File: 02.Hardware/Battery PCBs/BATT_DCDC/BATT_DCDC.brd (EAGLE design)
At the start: 30.4 x 23.5 mm, 66 parts, among them K3 FLEX8, Q1 NVTFS9D6P04M8LTAG, Q2 2N7002PW, Q5 2N7002PW, U1 MCP6071T-E/OT, U3 TPS55330RTET, U7 TPIC2810D

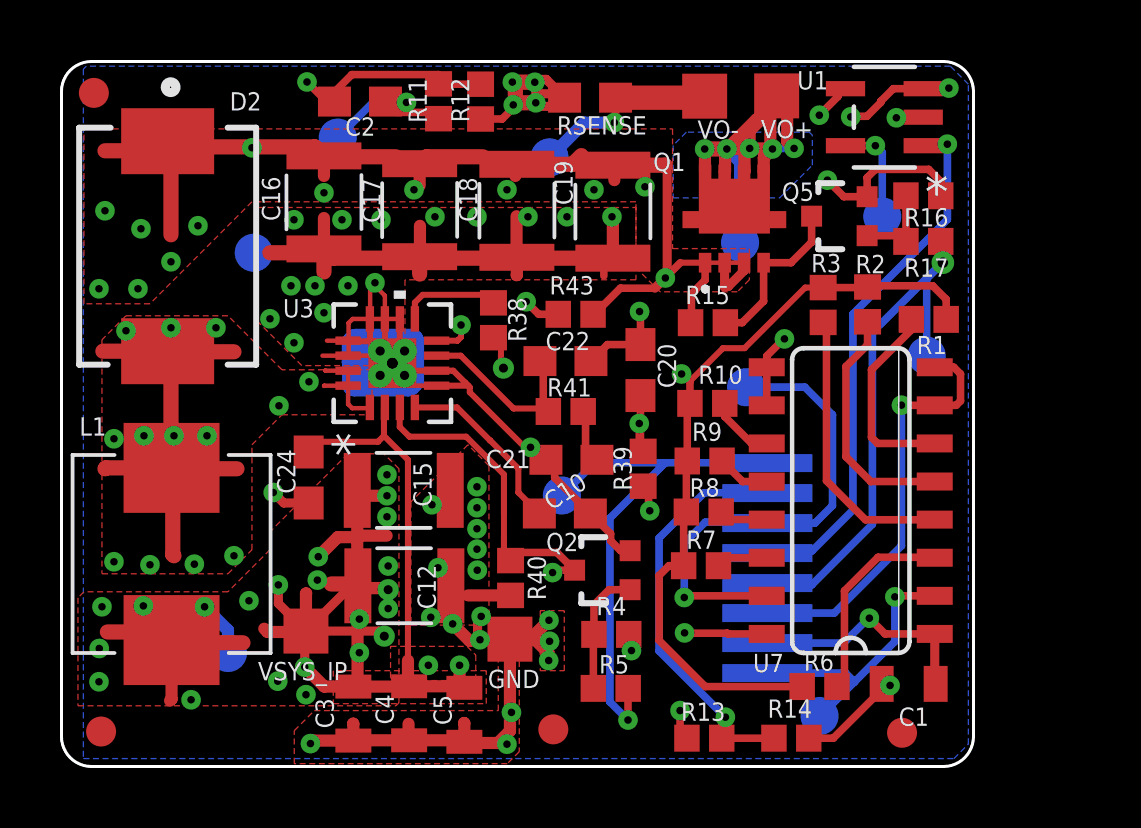
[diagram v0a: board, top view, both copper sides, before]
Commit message: Cambios revisados con David
Revision de los pcbs de la bateria.

En el DCDC se añade un diode Clamp (bat54s) en la medicion de la tension de salida.
Actualizacion de la BOM a v8.
Documentos de Cambios de versiones
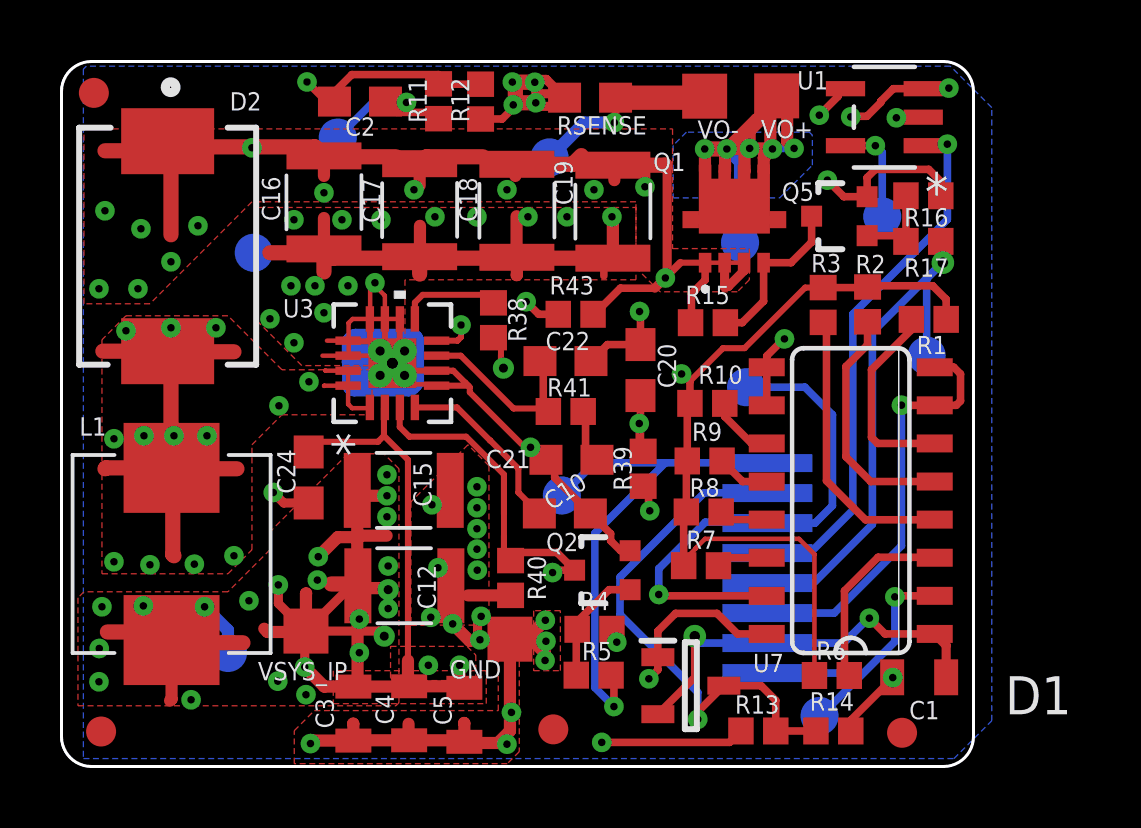
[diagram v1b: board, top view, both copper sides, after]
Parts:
- added D1: BAT54S, BAT54S:SOT95P240X110-3N
- R11: value 15k -> 5k1
- R12: value 1k -> 8k2
- RSENSE: value 10mR -> 100mR
- moved R13 1.82 mm to (44.8, 4.39)
- moved R14 1.42 mm to (47.3, 4.39)
- moved R5 0.72 mm to (39.3, 6.25)
- moved R4 0.59 mm to (39.3, 7.78)
- moved R6 0.55 mm to (47.2, 6.24)
- moved C1 0.41 mm to (50.1, 6.18)
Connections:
- net GND: now also D1.1
- net VCC: now also D1.2
- net VOUTSENSE: now also D1.3
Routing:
- net VOUT+: track 47.2 -> 55.9 mm
- net VCC: track 27.2 -> 32.7 mm, vias 2 -> 3
- net VOUTSENSE: track 13.6 -> 17.7 mm
- net GND: track 138.7 -> 140.5 mm
- net SCL: track 16.4 -> 17.5 mm

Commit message: Review final antes de produccion
-cambian valores de c10, r13, r15
-se añaden notas
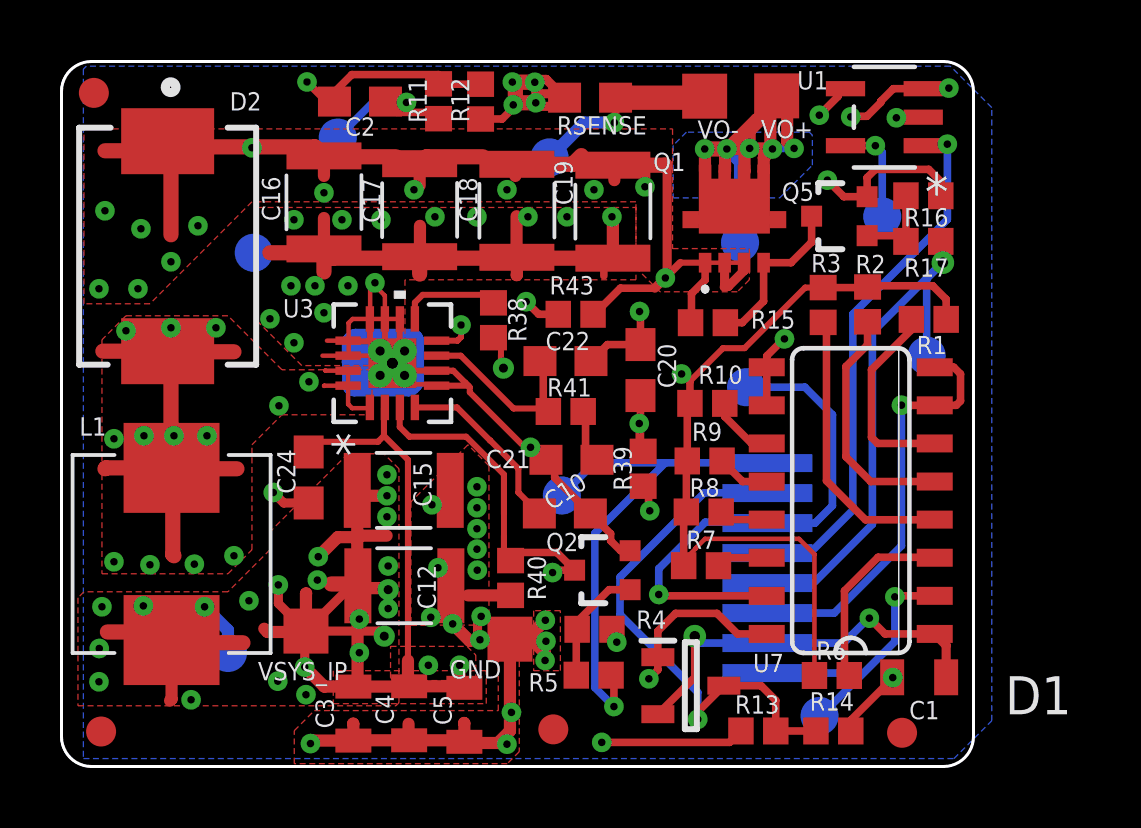
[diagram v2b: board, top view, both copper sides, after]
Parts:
- C20: value 47nF -> N.A.
- R13: value 150k -> 169k
- R15: value 470k -> 120k
- R40: value 78.7k -> N.A.
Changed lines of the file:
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@@
 <drawing>
 <settings>
-<setting alwaysvectorfont="no"/>
+<setting alwaysvectorfont="yes"/>
 <setting keepoldvectorfont="yes"/>
 <setting verticaltext="up"/>
@@
 <grid distance="0.01" unitdist="mm" unit="mm" style="lines" multiple="1" display="yes" altdistance="0.1" altunitdist="mm" altunit="mm"/>
 <layers>
-<layer number="1" name="Top" color="4" fill="1" visible="no" active="yes"/>
-<layer number="2" name="Route2" color="1" fill="3" visible="yes" active="yes"/>
+<layer number="1" name="Top" color="4" fill="1" visible="yes" active="yes"/>
+<layer number="2" name="Route2" color="1" fill="3" visible="no" active="yes"/>
 <layer number="3" name="Route3" color="4" fill="3" visible="no" active="no"/>
 <layer number="4" name="Route4" color="1" fill="4" visible="no" active="no"/>
@@
 <layer number="13" name="Route13" color="4" fill="5" visible="no" active="no"/>
 <layer number="14" name="Route14" color="1" fill="6" visible="no" active="no"/>
-<layer number="15" name="Route15" color="4" fill="6" visible="yes" active="yes"/>
+<layer number="15" name="Route15" color="4" fill="6" visible="no" active="yes"/>
 <layer number="16" name="Bottom" color="1" fill="1" visible="no" active="yes"/>
 <layer number="17" name="Pads" color="2" fill="1" visible="yes" active="yes"/>
@@
 <attribute name="PROD_ID" value=" " x="30.71" y="-53.71" size="1.778" layer="27" rot="R90" display="off"/>
 </element>
-<element name="R40" library="SparkFun-Resistors" library_urn="urn:adsk.eagle:library:532" package="0402" package3d_urn="urn:adsk.eagle:package:39657/1" value="78.7k" x="36.51" y="9.49" smashed="yes" rot="R270">
+<element name="R40" library="SparkFun-Resistors" library_urn="urn:adsk.eagle:library:532" package="0402" package3d_urn="urn:adsk.eagle:package:39657/1" value="N.A." x="36.51" y="9.49" smashed="yes" rot="R270">
 <attribute name="NAME" x="37.079" y="9.49" size="0.6096" layer="25" font="vector" rot="R270" align="bottom-center"/>
 <attribute name="PROD_ID" value=" " x="43.23" y="79.39" size="1.778" layer="27" rot="R270" display="off"/>
 </element>
-<element name="C20" library="SparkFun-Capacitors" package="0603" value="47nF" x="40.84" y="16.42" smashed="yes" rot="R90">
+<element name="C20" library="SparkFun-Capacitors" package="0603" value="N.A." x="40.84" y="16.42" smashed="yes" rot="R90">
 <attribute name="NAME" x="41.419" y="16.56" size="0.6096" layer="25" font="vector" rot="R270" align="bottom-center"/>
 <attribute name="PROD_ID" value="CAP-08605" x="41.4" y="-70.7" size="1.778" layer="27" rot="R90" display="off"/>
@@
 </element>
 <element name="R4" library="SparkFun-Resistors" library_urn="urn:adsk.eagle:library:532" package="0402" package3d_urn="urn:adsk.eagle:package:39657/1" value="470k" x="39.31" y="7.78" smashed="yes" rot="R180">
-<attribute name="NAME" x="39.31" y="8.419" size="0.6096" layer="25" font="vector" align="bottom-center"/>
+<attribute name="NAME" x="41.2" y="7.799" size="0.6096" layer="25" font="vector" align="bottom-center"/>
 <attribute name="PROD_ID" value=" " x="139.07" y="25.84" size="1.778" layer="27" rot="R180" display="off"/>
 </element>
 <element name="R5" library="SparkFun-Resistors" library_urn="urn:adsk.eagle:library:532" package="0402" package3d_urn="urn:adsk.eagle:package:39657/1" value="33" x="39.28" y="6.25" smashed="yes">
-<attribute name="NAME" x="39.39" y="6.749" size="0.6096" layer="25" font="vector" align="bottom-center"/>
+<attribute name="NAME" x="37.61" y="5.709" size="0.6096" layer="25" font="vector" align="bottom-center"/>
 <attribute name="PROD_ID" value=" " x="-63.54" y="-15.31" size="1.778" layer="27" display="off"/>
 </element>
@@
 <attribute name="VALUE" x="43.97" y="21.17" size="1.27" layer="27" font="vector" align="center"/>
 </element>
-<element name="R15" library="SparkFun-Resistors" library_urn="urn:adsk.eagle:library:532" package="0402" package3d_urn="urn:adsk.eagle:package:39657/1" value="470k" x="43.09" y="18" smashed="yes" rot="R180">
-<attribute name="NAME" x="43.08" y="18.622" size="0.6096" layer="25" font="vector" align="bottom-center"/>
+<element name="R15" library="SparkFun-Resistors" library_urn="urn:adsk.eagle:library:532" package="0402" package3d_urn="urn:adsk.eagle:package:39657/1" value="120k" x="43.09" y="18" smashed="yes" rot="R180">
+<attribute name="NAME" x="45.26" y="17.802" size="0.6096" layer="25" font="vector" align="bottom-center"/>
 <attribute name="PROD_ID" value=" " x="43.09" y="18" size="1.778" layer="27" rot="R180" display="off"/>
 <attribute name="VALUE" x="43.09" y="18.762" size="0.6096" layer="27" font="vector" rot="R180" align="top-center"/>
@@
 <attribute name="VALUE" x="39.16" y="24.738" size="0.6096" layer="27" font="vector" align="top-center"/>
 </element>
-<element name="R13" library="SparkFun-Resistors" library_urn="urn:adsk.eagle:library:532" package="0402" package3d_urn="urn:adsk.eagle:package:39657/1" value="150k" x="44.77" y="4.39" smashed="yes">
+<element name="R13" library="SparkFun-Resistors" library_urn="urn:adsk.eagle:library:532" package="0402" package3d_urn="urn:adsk.eagle:package:39657/1" value="169k" x="44.77" y="4.39" smashed="yes">
 <attribute name="NAME" x="44.73" y="5.578" size="0.6096" layer="25" font="vector" rot="R180" align="bottom-center"/>
 <attribute name="PROD_ID" value=" " x="44.77" y="4.39" size="1.778" layer="27" display="off"/>
